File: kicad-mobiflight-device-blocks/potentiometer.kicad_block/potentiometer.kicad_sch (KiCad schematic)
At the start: 2 parts

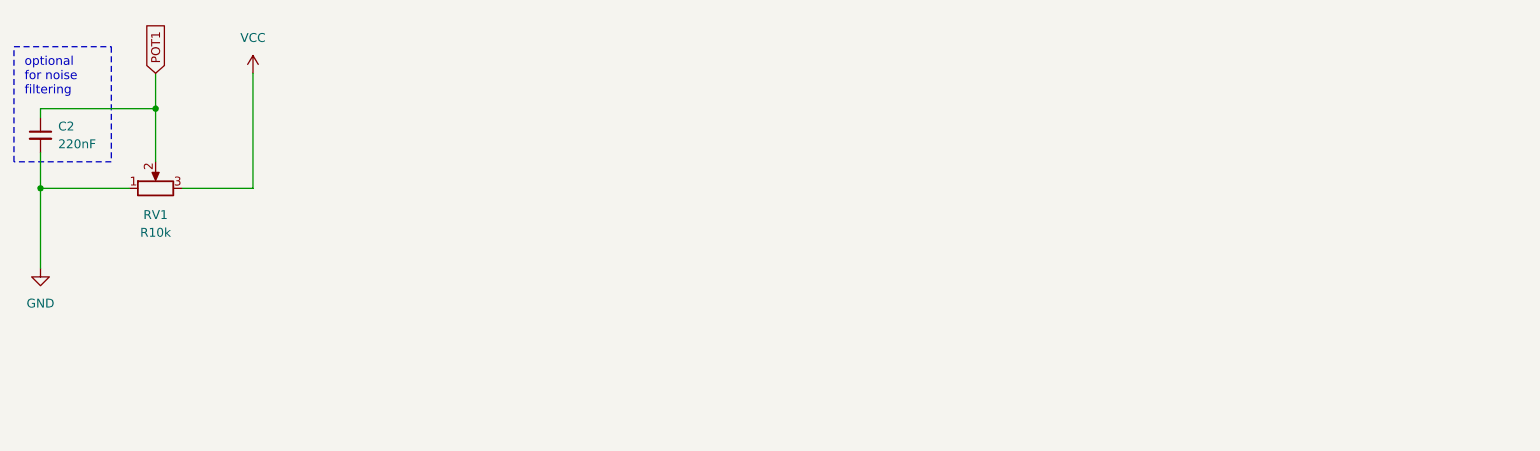
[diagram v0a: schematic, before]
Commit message: updated potentiometer design block to use the custom footprint
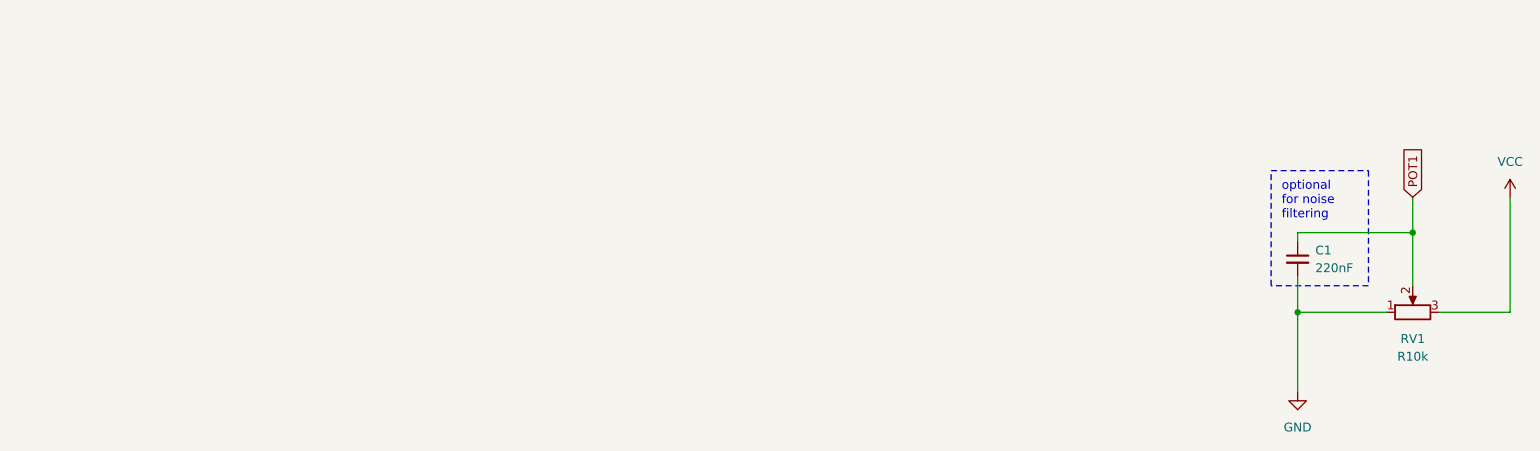
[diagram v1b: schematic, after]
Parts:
- RV1: footprint Potentiometer_THT:Potentiometer_Alps_RK09K_Single_Vertical -> MobiFlight-devices:Potentiometer_Alps_RK09K_Single_Vertical
- renumbered C2 to C1
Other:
- moved on the sheet: C1, RV1
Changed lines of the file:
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@@
 	(paper "A4")
 	(rectangle
-		(start 24.13 158.75)
-		(end 38.1 175.26)
+		(start 204.47 176.53)
+		(end 218.44 193.04)
 		(stroke
 			(width 0)
@@
 	(text "optional\nfor noise \nfiltering"
 		(exclude_from_sim no)
-		(at 25.654 160.274 0)
+		(at 205.994 178.054 0)
 		(effects
 			(font
@@
 	)
 	(junction
-		(at 27.94 179.07)
+		(at 208.28 196.85)
 		(diameter 0)
 		(color 0 0 0 0)
 	)
 	(junction
-		(at 44.45 167.64)
+		(at 224.79 185.42)
 		(diameter 0)
 		(color 0 0 0 0)
@@
 	(wire
 		(pts
-			(xy 27.94 173.99) (xy 27.94 179.07)
-		)
-		(stroke
-			(width 0)
-			(type default)
-		)
-	)
-	(wire
-		(pts
-			(xy 27.94 179.07) (xy 40.64 179.07)
-		)
-		(stroke
-			(width 0)
-			(type default)
-		)
-	)
-	(wire
-		(pts
-			(xy 27.94 167.64) (xy 27.94 168.91)
-		)
-		(stroke
-			(width 0)
-			(type default)
-		)
-	)
-	(wire
-		(pts
-			(xy 27.94 190.5) (xy 27.94 179.07)
-		)
-		(stroke
-			(width 0)
-			(type default)
-		)
-	)
-	(wire
-		(pts
-			(xy 44.45 162.56) (xy 44.45 167.64)
-		)
-		(stroke
-			(width 0)
-			(type default)
-		)
-	)
-	(wire
-		(pts
-			(xy 27.94 167.64) (xy 44.45 167.64)
-		)
-		(stroke
-			(width 0)
-			(type default)
-		)
-	)
-	(wire
-		(pts
-			(xy 58.42 162.56) (xy 58.42 179.07)
-		)
-		(stroke
-			(width 0)
-			(type default)
-		)
-	)
-	(wire
-		(pts
-			(xy 58.42 179.07) (xy 48.26 179.07)
-		)
-		(stroke
-			(width 0)
-			(type default)
-		)
-	)
-	(wire
-		(pts
-			(xy 44.45 167.64) (xy 44.45 175.26)
+			(xy 208.28 191.77) (xy 208.28 196.85)
+		)
+		(stroke
+			(width 0)
+			(type default)
+		)
+	)
+	(wire
+		(pts
+			(xy 208.28 196.85) (xy 220.98 196.85)
+		)
+		(stroke
+			(width 0)
+			(type default)
+		)
+	)
+	(wire
+		(pts
+			(xy 208.28 185.42) (xy 208.28 186.69)
+		)
+		(stroke
+			(width 0)
+			(type default)
+		)
+	)
+	(wire
+		(pts
+			(xy 208.28 208.28) (xy 208.28 196.85)
+		)
+		(stroke
+			(width 0)
+			(type default)
+		)
+	)
+	(wire
+		(pts
+			(xy 224.79 180.34) (xy 224.79 185.42)
+		)
+		(stroke
+			(width 0)
+			(type default)
+		)
+	)
+	(wire
+		(pts
+			(xy 208.28 185.42) (xy 224.79 185.42)
+		)
+		(stroke
+			(width 0)
+			(type default)
+		)
+	)
+	(wire
+		(pts
+			(xy 238.76 180.34) (xy 238.76 196.85)
+		)
+		(stroke
+			(width 0)
+			(type default)
+		)
+	)
+	(wire
+		(pts
+			(xy 238.76 196.85) (xy 228.6 196.85)
+		)
+		(stroke
+			(width 0)
+			(type default)
+		)
+	)
+	(wire
+		(pts
+			(xy 224.79 185.42) (xy 224.79 193.04)
 		)
 		(stroke
@@
 	(global_label "POT1"
 		(shape input)
-		(at 44.45 162.56 90)
+		(at 224.79 180.34 90)
 		(fields_autoplaced yes)
 		(effects
@@
 		)
 		(property "Intersheetrefs" "${INTERSHEET_REFS}"
-			(at 44.45 154.7972 90)
+			(at 224.79 172.5772 90)
 			(hide yes)
 			(show_name no)
@@
 	(symbol
 		(lib_id "Device:R_Potentiometer")
-		(at 44.45 179.07 90)
+		(at 224.79 196.85 90)
 		(unit 1)
 		(body_style 1)
@@
 		(dnp no)
 		(property "Reference" "RV1"
-			(at 44.45 182.88 90)
+			(at 224.79 200.66 90)
 			(show_name no)
 			(do_not_autoplace no)
@@
 		)
 		(property "Value" "R10k"
-			(at 44.45 185.42 90)
-			(show_name no)
-			(do_not_autoplace no)
-			(effects
-				(font
-					(size 1.27 1.27)
-				)
-			)
-		)
-		(property "Footprint" "Potentiometer_THT:Potentiometer_Alps_RK09K_Single_Vertical"
-			(at 44.45 179.07 0)
+			(at 224.79 203.2 90)
+			(show_name no)
+			(do_not_autoplace no)
+			(effects
+				(font
+					(size 1.27 1.27)
+				)
+			)
+		)
+		(property "Footprint" "MobiFlight-devices:Potentiometer_Alps_RK09K_Single_Vertical"
+			(at 224.79 196.85 0)
 			(hide yes)
 			(show_name no)
@@
 		)
 		(property "Datasheet" ""
-			(at 44.45 179.07 0)
+			(at 224.79 196.85 0)
 			(hide yes)
 			(show_name no)
@@
 		)
 		(property "Description" "Potentiometer"
-			(at 44.45 179.07 0)
+			(at 224.79 196.85 0)
 			(hide yes)
 			(show_name no)
@@
 	(symbol
 		(lib_id "power:GND")
-		(at 27.94 190.5 0)
+		(at 208.28 208.28 0)
 		(unit 1)
 		(body_style 1)
@@
 		(fields_autoplaced yes)
 		(property "Reference" "#PWR01"
-			(at 27.94 196.85 0)
+			(at 208.28 214.63 0)
 			(hide yes)
 			(show_name no)
@@
 		)
 		(property "Value" "GND"
-			(at 27.94 195.58 0)
+			(at 208.28 213.36 0)
 			(show_name no)
 			(do_not_autoplace no)
@@
 		)
 		(property "Footprint" ""
-			(at 27.94 190.5 0)
+			(at 208.28 208.28 0)
 			(hide yes)
 			(show_name no)
@@
 		)
 		(property "Datasheet" ""
-			(at 27.94 190.5 0)
+			(at 208.28 208.28 0)
 			(hide yes)
 			(show_name no)
@@
 		)
 		(property "Description" "Power symbol creates a global label with name \"GND\" , ground"
-			(at 27.94 190.5 0)
+			(at 208.28 208.28 0)
 			(hide yes)
 			(show_name no)
@@
 	(symbol
 		(lib_id "power:VCC")
-		(at 58.42 162.56 0)
+		(at 238.76 180.34 0)
 		(unit 1)
 		(body_style 1)
@@
 		(fields_autoplaced yes)
 		(property "Reference" "#PWR02"
-			(at 58.42 166.37 0)
+			(at 238.76 184.15 0)
 			(hide yes)
 			(show_name no)
@@
 		)
 		(property "Value" "VCC"
-			(at 58.42 157.48 0)
+			(at 238.76 175.26 0)
 			(show_name no)
 			(do_not_autoplace no)
@@
 		)
 		(property "Footprint" ""
-			(at 58.42 162.56 0)
+			(at 238.76 180.34 0)
 			(hide yes)
 			(show_name no)
@@
 		)
 		(property "Datasheet" ""
-			(at 58.42 162.56 0)
+			(at 238.76 180.34 0)
 			(hide yes)
 			(show_name no)
@@
 		)
 		(property "Description" "Power symbol creates a global label with name \"VCC\""
-			(at 58.42 162.56 0)
+			(at 238.76 180.34 0)
 			(hide yes)
 			(show_name no)
@@
 	(symbol
 		(lib_id "Device:C_Small")
-		(at 27.94 171.45 0)
+		(at 208.28 189.23 0)
 		(unit 1)
 		(body_style 1)
@@
 		(dnp no)
 		(fields_autoplaced yes)
-		(property "Reference" "C2"
-			(at 30.48 170.1862 0)
+		(property "Reference" "C1"
+			(at 210.82 187.9662 0)
 			(show_name no)
 			(do_not_autoplace no)
@@
 		)
 		(property "Value" "220nF"
-			(at 30.48 172.7262 0)
+			(at 210.82 190.5062 0)
 			(show_name no)
 			(do_not_autoplace no)
@@
 		)
 		(property "Footprint" "Capacitor_THT:C_Disc_D7.0mm_W2.5mm_P5.00mm"
-			(at 27.94 171.45 0)
+			(at 208.28 189.23 0)
 			(hide yes)
 			(show_name no)
@@
 		)
 		(property "Datasheet" ""
-			(at 27.94 171.45 0)
+			(at 208.28 189.23 0)
 			(hide yes)
 			(show_name no)
@@
 		)
 		(property "Description" "Unpolarized capacitor, small symbol"
-			(at 27.94 171.45 0)
+			(at 208.28 189.23 0)
 			(hide yes)
 			(show_name no)
@@
 			(project "kicad-mobiflight-device-blocks-worksheet"
 				(path "/4714e232-3dfb-45f4-a0c3-3539b78f5138"
-					(reference "C2")
+					(reference "C1")
 					(unit 1)
 				)
